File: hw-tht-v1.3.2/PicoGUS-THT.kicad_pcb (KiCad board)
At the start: 2 copper layers, 103.7 x 99.8 mm, 88 parts, among them J1 IRQDMA_JP, J11 USB-A, J3 Bus_ISA_8bit, J5 SJ1-3535NG, J6 UART_TX, J7 USB power jumper, J8 SJ1-3535NG-GR, J9 Waveblaster, U1 Pico, U10 74AHCT126, U11 NE5532, U12 USBLC6-2SC6, U2 74AHC244, U3 SN74CB3T3257, U4 SN74CB3T3257, U5 74AHC14, U6 74AHC00, U7 74AHC00, U8 APS6404L-3SQR-SN, U9 PCM5100A

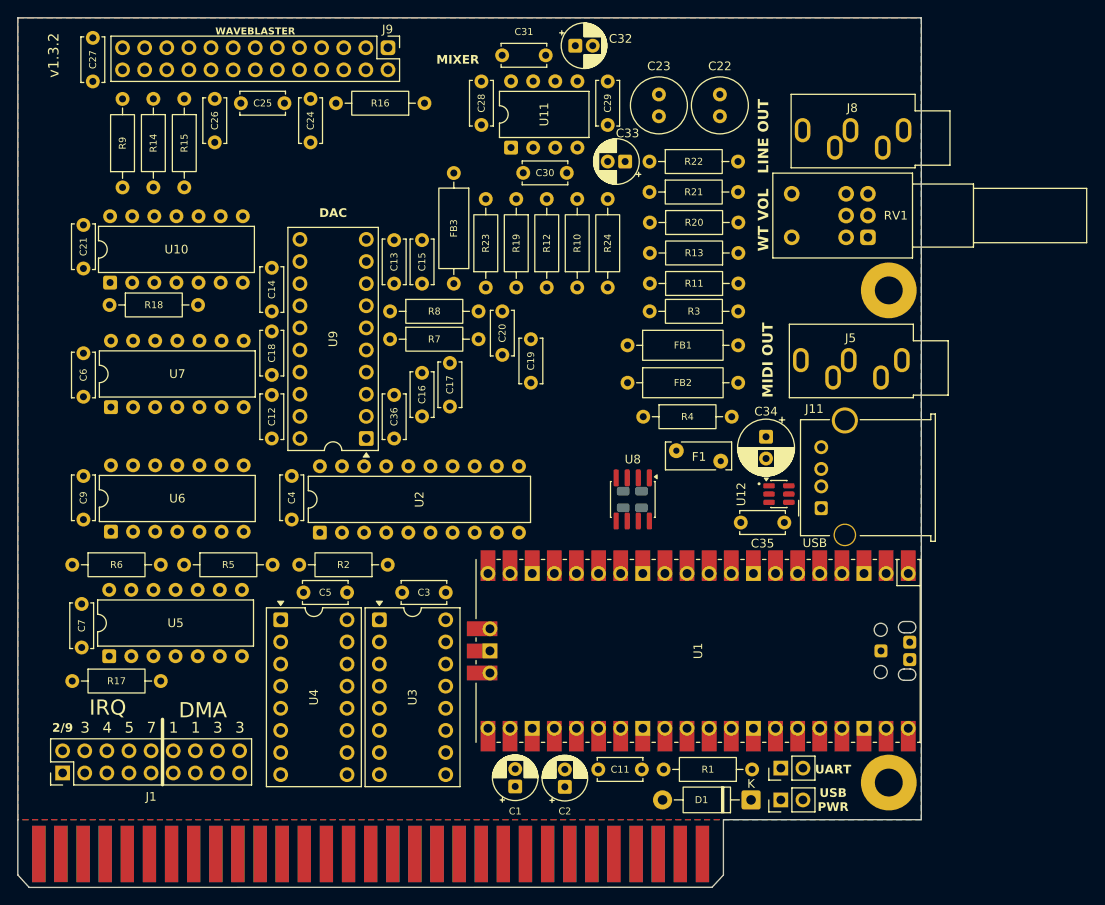
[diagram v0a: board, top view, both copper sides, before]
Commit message: THT v1.3.2: routed board (user's arrangement), QC fixes applied
The user's final placement (logic column at the left edge, U2 lower left,
J1 at x 120, horizontal U9 DIP-20, U3/U4 swapped, U12/F1/U8 rearranged),
routed and reviewed against v1.3.1 (analog/power, digital/ISA/USB, DFM,
silkscreen), with the verified fixes applied:

- +5V out of the J9 rows and away from C27.1 (-12V); +12V centred necks
  through the U2 pin rows; -12V necks between U9 GND pins at 0.32 mm
- USB-host +5V feed re-routed: no +5V/+-12V within 0.30 mm of a Pico pad,
  clear of J11's pins and the Pico test pads
- Pico test-pad rule areas and USB relief slots follow U1's 0.27 mm move
- J9 ground stitching, via nudges off pads, castellations and fingers,
  router debris removed, via joins re-centred
- Princess art re-placed (53 mm), back text re-spaced, C8/C10 back
  references beside their caps, stray U12 pin-1 dot removed

DRC with schematic parity: 0 errors, 0 unconnected.

Co-Authored-By: Claude Opus 5.5 <noreply@anthropic.com>
Claude-Session: https://claude.ai/code/session_011utN3x8yYUNDvkpGCEq5yD
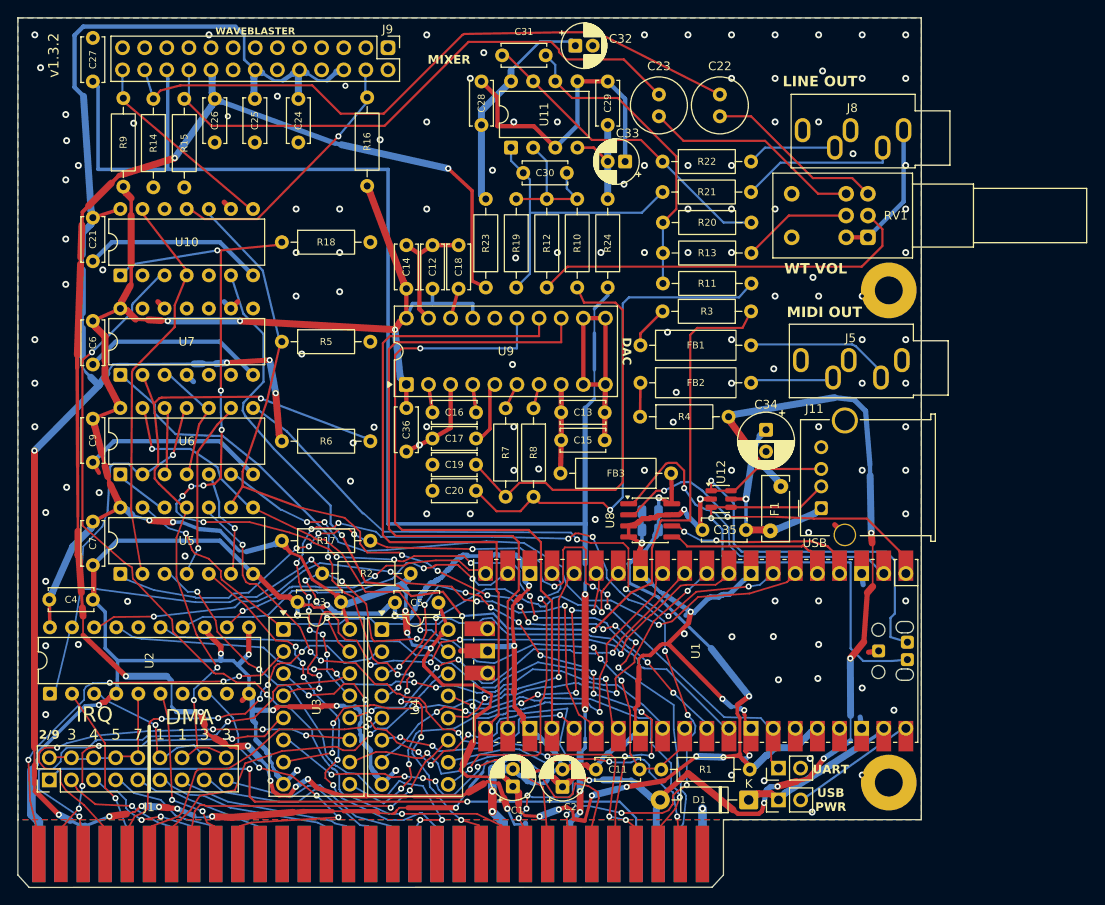
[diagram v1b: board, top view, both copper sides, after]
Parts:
- moved FB3 42.6 mm to (191.4, 88.5), turned to 180 degrees
- moved U2 36.1 mm to (120.1, 113.8)
- moved C4 31.3 mm to (120.0, 103.0), turned to 0 degrees
- moved C13 31.2 mm to (183.8, 81.5), turned to 180 degrees
- moved R17 29.0 mm to (146.7, 96.2)
- moved R5 28.0 mm to (146.7, 73.4)
- moved R6 27.9 mm to (146.7, 84.8)
- moved C12 25.2 mm to (164.0, 62.3)
- moved C15 24.1 mm to (178.8, 84.7), turned to 0 degrees
- moved C18 23.6 mm to (167.0, 67.3)
- moved R18 21.1 mm to (146.7, 62.0)
- moved R8 19.9 mm to (175.6, 81.0), turned to -90 degrees
- moved C20 17.5 mm to (164.0, 90.5), turned to 0 degrees
- moved C14 15.7 mm to (161.0, 62.3)
- moved R7 15.5 mm to (172.4, 81.0), turned to -90 degrees
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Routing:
- net GND: track 0.00 -> 501.6 mm, vias 0 -> 145
- net +5V: track 0.00 -> 352.1 mm, vias 0 -> 19
- net +3V3: track 0.00 -> 305.9 mm, vias 0 -> 16
- net +12V: track 0.00 -> 186.9 mm, vias 0 -> 9
- net -12V: track 0.00 -> 185.3 mm, vias 0 -> 4
- net ~{RI/OCHRDY}: track 0.00 -> 125.3 mm, vias 0 -> 14
- net Net-(R3-Pad1): track 0.00 -> 120.5 mm, vias 0 -> 3
- net RESET: track 0.00 -> 118.7 mm, vias 0 -> 9
- net D2: track 0.00 -> 109.5 mm, vias 0 -> 15
- net ~{BUSOE}: track 0.00 -> 103.6 mm, vias 0 -> 7
- net UART_TX: track 0.00 -> 101.9 mm, vias 0 -> 9
- net I/OCHRDY: track 0.00 -> 101.0 mm, vias 0 -> 3
- net RUN: track 0.00 -> 90.7 mm, vias 0 -> 5
- net BCK: track 0.00 -> 81.0 mm
- net ADS: track 0.00 -> 80.3 mm, vias 0 -> 1
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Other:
- outline, holes or cut-outs redrawn
